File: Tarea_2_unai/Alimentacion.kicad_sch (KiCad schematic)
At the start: 4 parts, among them J1 Conn_01x02_Pin, U1 AMS1117-3.3

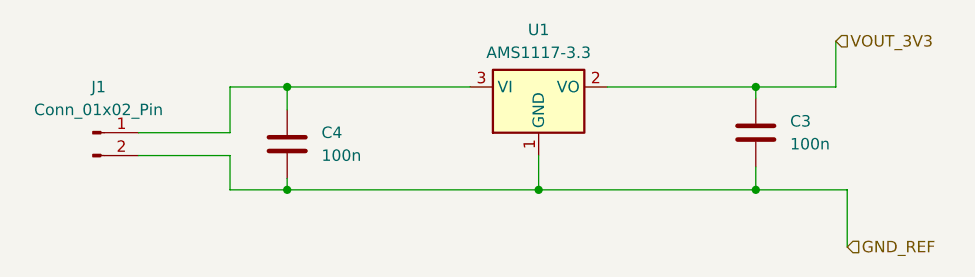
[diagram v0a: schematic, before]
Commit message: Tarea_3
Falta el enrutado y configuraciones Configurar el Clearance a 0.2mm y Track Width
/ Track Distance mínimos a 0.25mm
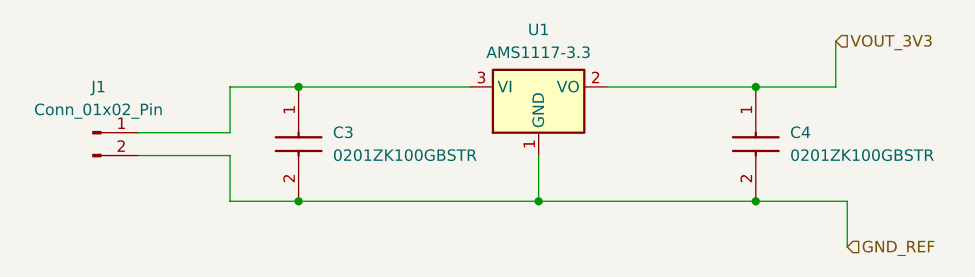
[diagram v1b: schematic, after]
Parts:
- removed C3, C4: 100n, 0201ZK100GBSTR, symbol Device:C
- added C3, C4: 0201ZK100GBSTR, CAPC0603X28N, symbol 0201ZK100GBSTR:0201ZK100GBSTR
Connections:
- net GND_REF: now also C3.2, C4.2
- net VOUT_3V3: now also C4.1
- net at J1.1 (Pin_1), U1.3 (VI): now also C3.1
